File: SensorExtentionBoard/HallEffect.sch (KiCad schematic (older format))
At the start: 11 parts, among them J5 Conn_01x03_Male, J6 Conn_01x03_Male, J7 Conn_01x03_Male, U3 ADS1015IDGS

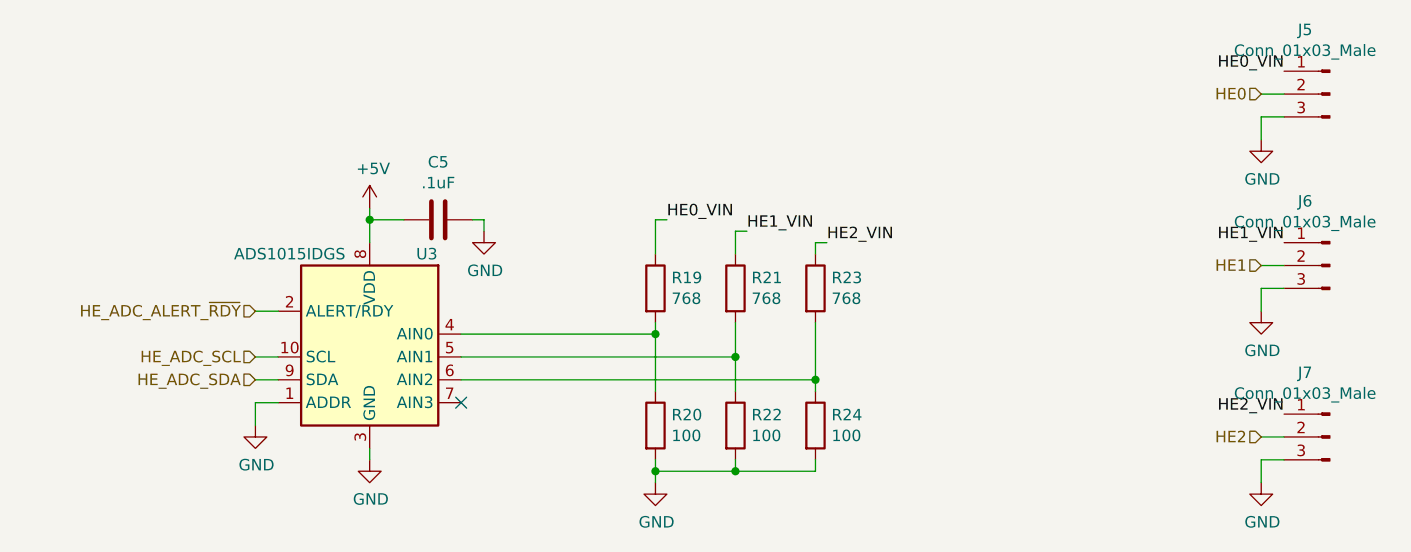
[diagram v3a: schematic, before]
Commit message: Replaced ADS1115 with ADS1015 on PT page
The ADS1115 is being used to read the voltages provided by the Helix
system to the pressure transducers. The ADS1015 is already doing
the same job for the Hall Effect sensors, however the ADS1015 has
4 bits lower accuracy. High accuracy is not needed for this
application so be replacing the ADS1115 with the ADS1015 we can
reduce cost and more importantly reduce BOM size making the project
logistics easier to manage.
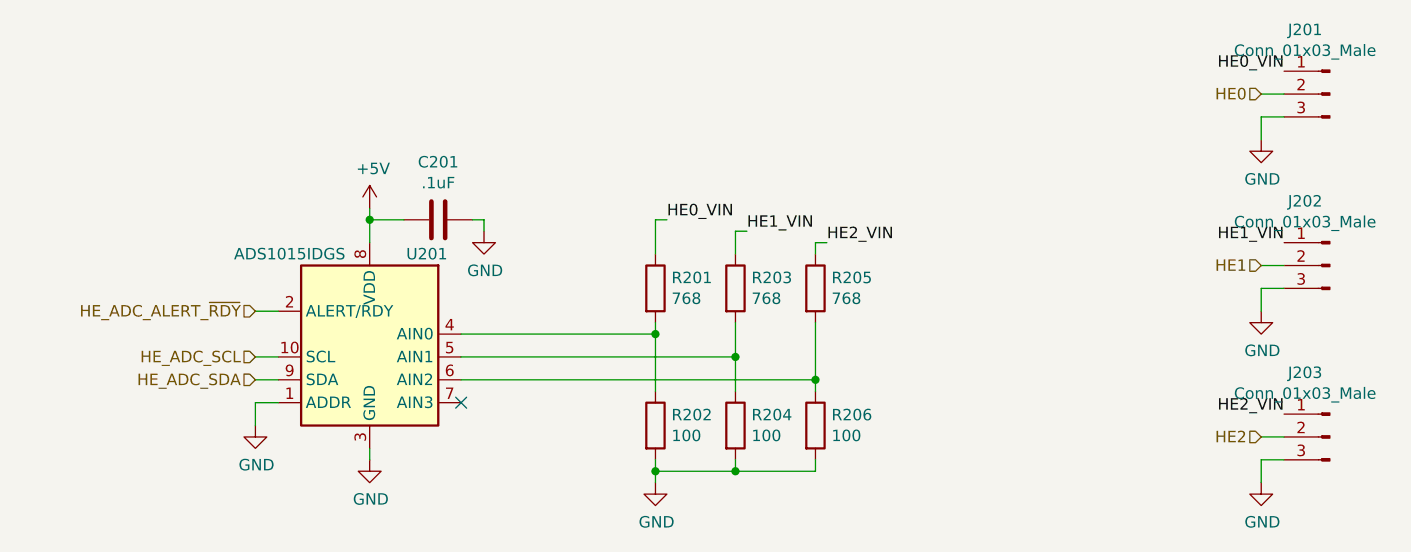
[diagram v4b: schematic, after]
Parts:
- renumbered C5 to C201, J5 to J201, J6 to J202, J7 to J203, R19 to R201, R20 to R202, R21 to R203, R22 to R204, R23 to R205, R24 to R206, U3 to U201
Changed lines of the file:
@@
 $EndDescr
 $Comp
-L Connector:Conn_01x03_Male J5
+L Connector:Conn_01x03_Male J201
 U 1 1 5E39E325
 P 8450 2100
-F 0 "J5" H 8558 2381 50  0000 C CNN
+F 0 "J201" H 8558 2381 50  0000 C CNN
 F 1 "Conn_01x03_Male" H 8558 2290 50  0000 C CNN
 F 2 "Connector_Molex:Molex_MicroClasp_55932-0310_1x03_P2.00mm_Vertical" H 8450 2100 50  0001 C CNN
@@
 $EndComp
 $Comp
-L Analog_ADC:ADS1015IDGS U3
+L Analog_ADC:ADS1015IDGS U201
 U 1 1 5E39F012
 P 4250 3250
-F 0 "U3" H 4000 3700 50  0000 C CNN
+F 0 "U201" H 4000 3700 50  0000 C CNN
 F 1 "ADS1015IDGS" H 4600 3700 50  0000 C CNN
 F 2 "Package_SO:TSSOP-10_3x3mm_P0.5mm" H 4250 2750 50  0001 C CNN
@@
 	8150 2100 8250 2100
 $Comp
-L power:GND #PWR021
+L power:GND #PWR0206
 U 1 1 5E3A1F0E
 P 8150 2300
-F 0 "#PWR021" H 8150 2050 50  0001 C CNN
+F 0 "#PWR0206" H 8150 2050 50  0001 C CNN
 F 1 "GND" H 8155 2127 50  0000 C CNN
 F 2 "" H 8150 2300 50  0001 C CNN
@@
 HE0_VIN
 $Comp
-L Connector:Conn_01x03_Male J6
+L Connector:Conn_01x03_Male J202
 U 1 1 5E3A451B
 P 8450 2850
-F 0 "J6" H 8558 3131 50  0000 C CNN
+F 0 "J202" H 8558 3131 50  0000 C CNN
 F 1 "Conn_01x03_Male" H 8558 3040 50  0000 C CNN
 F 2 "Connector_Molex:Molex_MicroClasp_55932-0310_1x03_P2.00mm_Vertical" H 8450 2850 50  0001 C CNN
@@
 	8150 2850 8250 2850
 $Comp
-L power:GND #PWR022
+L power:GND #PWR0207
 U 1 1 5E3A4523
 P 8150 3050
-F 0 "#PWR022" H 8150 2800 50  0001 C CNN
+F 0 "#PWR0207" H 8150 2800 50  0001 C CNN
 F 1 "GND" H 8155 2877 50  0000 C CNN
 F 2 "" H 8150 3050 50  0001 C CNN
@@
 HE1_VIN
 $Comp
-L Connector:Conn_01x03_Male J7
+L Connector:Conn_01x03_Male J203
 U 1 1 5E3A51E7
 P 8450 3600
-F 0 "J7" H 8558 3881 50  0000 C CNN
+F 0 "J203" H 8558 3881 50  0000 C CNN
 F 1 "Conn_01x03_Male" H 8558 3790 50  0000 C CNN
 F 2 "Connector_Molex:Molex_MicroClasp_55932-0310_1x03_P2.00mm_Vertical" H 8450 3600 50  0001 C CNN
@@
 	8150 3600 8250 3600
 $Comp
-L power:GND #PWR023
+L power:GND #PWR0208
 U 1 1 5E3A51EF
 P 8150 3800
-F 0 "#PWR023" H 8150 3550 50  0001 C CNN
+F 0 "#PWR0208" H 8150 3550 50  0001 C CNN
 F 1 "GND" H 8155 3627 50  0000 C CNN
 F 2 "" H 8150 3800 50  0001 C CNN
@@
 HE2_VIN
 $Comp
-L power:GND #PWR018
+L power:GND #PWR0203
 U 1 1 5E3A708B
 P 4250 3700
-F 0 "#PWR018" H 4250 3450 50  0001 C CNN
+F 0 "#PWR0203" H 4250 3450 50  0001 C CNN
 F 1 "GND" H 4255 3527 50  0000 C CNN
 F 2 "" H 4250 3700 50  0001 C CNN
@@
 	4250 3700 4250 3650
 $Comp
-L power:GND #PWR016
+L power:GND #PWR0201
 U 1 1 5E3A756C
 P 3750 3550
-F 0 "#PWR016" H 3750 3300 50  0001 C CNN
+F 0 "#PWR0201" H 3750 3300 50  0001 C CNN
 F 1 "GND" H 3755 3377 50  0000 C CNN
 F 2 "" H 3750 3550 50  0001 C CNN
@@
 Connection ~ 6200 3350
 $Comp
-L power:GND #PWR020
+L power:GND #PWR0205
 U 1 1 5E3B85EB
 P 5500 3800
-F 0 "#PWR020" H 5500 3550 50  0001 C CNN
+F 0 "#PWR0205" H 5500 3550 50  0001 C CNN
 F 1 "GND" H 5505 3627 50  0000 C CNN
 F 2 "" H 5500 3800 50  0001 C CNN
@@
 	5500 2650 5500 2800
 $Comp
-L power:+5V #PWR017
+L power:+5V #PWR0202
 U 1 1 5E3C2F7A
 P 4250 2600
-F 0 "#PWR017" H 4250 2450 50  0001 C CNN
+F 0 "#PWR0202" H 4250 2450 50  0001 C CNN
 F 1 "+5V" H 4265 2773 50  0000 C CNN
 F 2 "" H 4250 2600 50  0001 C CNN
@@
 P 5500 3550
 AR Path="/5E628041" Ref="R?"  Part="1"
-AR Path="/5E059E7A/5E628041" Ref="R20"  Part="1"
-F 0 "R20" H 5570 3596 50  0000 L CNN
+AR Path="/5E059E7A/5E628041" Ref="R202"  Part="1"
+F 0 "R202" H 5570 3596 50  0000 L CNN
 F 1 "100" H 5570 3505 50  0000 L CNN
 F 2 "Resistor_SMD:R_1206_3216Metric_Pad1.42x1.75mm_HandSolder" V 5430 3550 50  0001 C CNN
@@
 P 6200 2950
 AR Path="/5E059EAC/5E63C1A6" Ref="R?"  Part="1"
-AR Path="/5E059E7A/5E63C1A6" Ref="R23"  Part="1"
-F 0 "R23" H 6270 2996 50  0000 L CNN
+AR Path="/5E059E7A/5E63C1A6" Ref="R205"  Part="1"
+F 0 "R205" H 6270 2996 50  0000 L CNN
 F 1 "768" H 6270 2905 50  0000 L CNN
 F 2 "Resistor_SMD:R_1206_3216Metric_Pad1.42x1.75mm_HandSolder" V 6130 2950 50  0001 C CNN
@@
 P 5850 2950
 AR Path="/5E059EAC/5E63F6B5" Ref="R?"  Part="1"
-AR Path="/5E059E7A/5E63F6B5" Ref="R21"  Part="1"
-F 0 "R21" H 5920 2996 50  0000 L CNN
+AR Path="/5E059E7A/5E63F6B5" Ref="R203"  Part="1"
+F 0 "R203" H 5920 2996 50  0000 L CNN
 F 1 "768" H 5920 2905 50  0000 L CNN
 F 2 "Resistor_SMD:R_1206_3216Metric_Pad1.42x1.75mm_HandSolder" V 5780 2950 50  0001 C CNN
@@
 P 5500 2950
 AR Path="/5E059EAC/5E63FA92" Ref="R?"  Part="1"
-AR Path="/5E059E7A/5E63FA92" Ref="R19"  Part="1"
-F 0 "R19" H 5570 2996 50  0000 L CNN
+AR Path="/5E059E7A/5E63FA92" Ref="R201"  Part="1"
+F 0 "R201" H 5570 2996 50  0000 L CNN
 F 1 "768" H 5570 2905 50  0000 L CNN
 F 2 "Resistor_SMD:R_1206_3216Metric_Pad1.42x1.75mm_HandSolder" V 5430 2950 50  0001 C CNN
@@
 P 5850 3550
 AR Path="/5E6458A4" Ref="R?"  Part="1"
-AR Path="/5E059E7A/5E6458A4" Ref="R22"  Part="1"
-F 0 "R22" H 5920 3596 50  0000 L CNN
+AR Path="/5E059E7A/5E6458A4" Ref="R204"  Part="1"
+F 0 "R204" H 5920 3596 50  0000 L CNN
 F 1 "100" H 5920 3505 50  0000 L CNN
 F 2 "Resistor_SMD:R_1206_3216Metric_Pad1.42x1.75mm_HandSolder" V 5780 3550 50  0001 C CNN
@@
 P 6200 3550
 AR Path="/5E645AA9" Ref="R?"  Part="1"
-AR Path="/5E059E7A/5E645AA9" Ref="R24"  Part="1"
-F 0 "R24" H 6270 3596 50  0000 L CNN
+AR Path="/5E059E7A/5E645AA9" Ref="R206"  Part="1"
+F 0 "R206" H 6270 3596 50  0000 L CNN
 F 1 "100" H 6270 3505 50  0000 L CNN
 F 2 "Resistor_SMD:R_1206_3216Metric_Pad1.42x1.75mm_HandSolder" V 6130 3550 50  0001 C CNN
@@
 P 4550 2650
 AR Path="/5E24F640" Ref="C?"  Part="1"
-AR Path="/5E059E7A/5E24F640" Ref="C5"  Part="1"
-F 0 "C5" V 4298 2650 50  0000 C CNN
+AR Path="/5E059E7A/5E24F640" Ref="C201"  Part="1"
+F 0 "C201" V 4298 2650 50  0000 C CNN
 F 1 ".1uF" V 4389 2650 50  0000 C CNN
 F 2 "" H 4588 2500 50  0001 C CNN
@@
 P 4750 2700
 AR Path="/5E24F646" Ref="#PWR?"  Part="1"
-AR Path="/5E059E7A/5E24F646" Ref="#PWR019"  Part="1"
-F 0 "#PWR019" H 4750 2450 50  0001 C CNN
+AR Path="/5E059E7A/5E24F646" Ref="#PWR0204"  Part="1"
+F 0 "#PWR0204" H 4750 2450 50  0001 C CNN
 F 1 "GND" H 4755 2527 50  0000 C CNN
 F 2 "" H 4750 2700 50  0001 C CNN

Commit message: Added header for programming the EEPROM memory on the SEB
Adding this header may allow the test rig to load new memory configs
onto the SEB under test prior to running tests. This will allow
greater ability for automation of testing when the new software
requires a change to the config onboard the SEB.
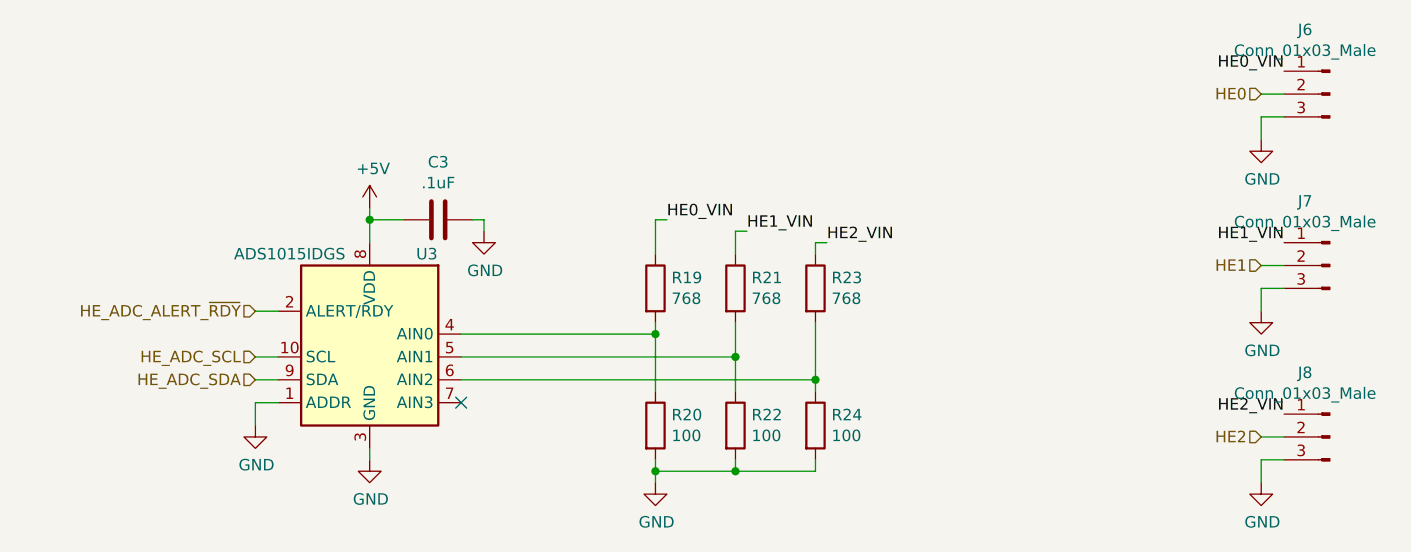
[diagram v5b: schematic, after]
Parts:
- renumbered C201 to C3, J201 to J6, J202 to J7, J203 to J8, R201 to R19, R202 to R20, R203 to R21, R204 to R22, R205 to R23, R206 to R24, U201 to U3
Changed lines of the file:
@@
 $EndDescr
 $Comp
-L Connector:Conn_01x03_Male J201
+L Connector:Conn_01x03_Male J6
 U 1 1 5E39E325
 P 8450 2100
-F 0 "J201" H 8558 2381 50  0000 C CNN
+F 0 "J6" H 8558 2381 50  0000 C CNN
 F 1 "Conn_01x03_Male" H 8558 2290 50  0000 C CNN
 F 2 "Connector_Molex:Molex_MicroClasp_55932-0310_1x03_P2.00mm_Vertical" H 8450 2100 50  0001 C CNN
@@
 $EndComp
 $Comp
-L Analog_ADC:ADS1015IDGS U201
+L Analog_ADC:ADS1015IDGS U3
 U 1 1 5E39F012
 P 4250 3250
-F 0 "U201" H 4000 3700 50  0000 C CNN
+F 0 "U3" H 4000 3700 50  0000 C CNN
 F 1 "ADS1015IDGS" H 4600 3700 50  0000 C CNN
 F 2 "Package_SO:TSSOP-10_3x3mm_P0.5mm" H 4250 2750 50  0001 C CNN
@@
 	8150 2100 8250 2100
 $Comp
-L power:GND #PWR0206
+L power:GND #PWR024
 U 1 1 5E3A1F0E
 P 8150 2300
-F 0 "#PWR0206" H 8150 2050 50  0001 C CNN
+F 0 "#PWR024" H 8150 2050 50  0001 C CNN
 F 1 "GND" H 8155 2127 50  0000 C CNN
 F 2 "" H 8150 2300 50  0001 C CNN
@@
 HE0_VIN
 $Comp
-L Connector:Conn_01x03_Male J202
+L Connector:Conn_01x03_Male J7
 U 1 1 5E3A451B
 P 8450 2850
-F 0 "J202" H 8558 3131 50  0000 C CNN
+F 0 "J7" H 8558 3131 50  0000 C CNN
 F 1 "Conn_01x03_Male" H 8558 3040 50  0000 C CNN
 F 2 "Connector_Molex:Molex_MicroClasp_55932-0310_1x03_P2.00mm_Vertical" H 8450 2850 50  0001 C CNN
@@
 	8150 2850 8250 2850
 $Comp
-L power:GND #PWR0207
+L power:GND #PWR025
 U 1 1 5E3A4523
 P 8150 3050
-F 0 "#PWR0207" H 8150 2800 50  0001 C CNN
+F 0 "#PWR025" H 8150 2800 50  0001 C CNN
 F 1 "GND" H 8155 2877 50  0000 C CNN
 F 2 "" H 8150 3050 50  0001 C CNN
@@
 HE1_VIN
 $Comp
-L Connector:Conn_01x03_Male J203
+L Connector:Conn_01x03_Male J8
 U 1 1 5E3A51E7
 P 8450 3600
-F 0 "J203" H 8558 3881 50  0000 C CNN
+F 0 "J8" H 8558 3881 50  0000 C CNN
 F 1 "Conn_01x03_Male" H 8558 3790 50  0000 C CNN
 F 2 "Connector_Molex:Molex_MicroClasp_55932-0310_1x03_P2.00mm_Vertical" H 8450 3600 50  0001 C CNN
@@
 	8150 3600 8250 3600
 $Comp
-L power:GND #PWR0208
+L power:GND #PWR026
 U 1 1 5E3A51EF
 P 8150 3800
-F 0 "#PWR0208" H 8150 3550 50  0001 C CNN
+F 0 "#PWR026" H 8150 3550 50  0001 C CNN
 F 1 "GND" H 8155 3627 50  0000 C CNN
 F 2 "" H 8150 3800 50  0001 C CNN
@@
 HE2_VIN
 $Comp
-L power:GND #PWR0203
+L power:GND #PWR021
 U 1 1 5E3A708B
 P 4250 3700
-F 0 "#PWR0203" H 4250 3450 50  0001 C CNN
+F 0 "#PWR021" H 4250 3450 50  0001 C CNN
 F 1 "GND" H 4255 3527 50  0000 C CNN
 F 2 "" H 4250 3700 50  0001 C CNN
@@
 	4250 3700 4250 3650
 $Comp
-L power:GND #PWR0201
+L power:GND #PWR019
 U 1 1 5E3A756C
 P 3750 3550
-F 0 "#PWR0201" H 3750 3300 50  0001 C CNN
+F 0 "#PWR019" H 3750 3300 50  0001 C CNN
 F 1 "GND" H 3755 3377 50  0000 C CNN
 F 2 "" H 3750 3550 50  0001 C CNN
@@
 Connection ~ 6200 3350
 $Comp
-L power:GND #PWR0205
+L power:GND #PWR023
 U 1 1 5E3B85EB
 P 5500 3800
-F 0 "#PWR0205" H 5500 3550 50  0001 C CNN
+F 0 "#PWR023" H 5500 3550 50  0001 C CNN
 F 1 "GND" H 5505 3627 50  0000 C CNN
 F 2 "" H 5500 3800 50  0001 C CNN
@@
 	5500 2650 5500 2800
 $Comp
-L power:+5V #PWR0202
+L power:+5V #PWR020
 U 1 1 5E3C2F7A
 P 4250 2600
-F 0 "#PWR0202" H 4250 2450 50  0001 C CNN
+F 0 "#PWR020" H 4250 2450 50  0001 C CNN
 F 1 "+5V" H 4265 2773 50  0000 C CNN
 F 2 "" H 4250 2600 50  0001 C CNN
@@
 P 5500 3550
 AR Path="/5E628041" Ref="R?"  Part="1"
-AR Path="/5E059E7A/5E628041" Ref="R202"  Part="1"
-F 0 "R202" H 5570 3596 50  0000 L CNN
+AR Path="/5E059E7A/5E628041" Ref="R20"  Part="1"
+F 0 "R20" H 5570 3596 50  0000 L CNN
 F 1 "100" H 5570 3505 50  0000 L CNN
 F 2 "Resistor_SMD:R_1206_3216Metric_Pad1.42x1.75mm_HandSolder" V 5430 3550 50  0001 C CNN
@@
 P 6200 2950
 AR Path="/5E059EAC/5E63C1A6" Ref="R?"  Part="1"
-AR Path="/5E059E7A/5E63C1A6" Ref="R205"  Part="1"
-F 0 "R205" H 6270 2996 50  0000 L CNN
+AR Path="/5E059E7A/5E63C1A6" Ref="R23"  Part="1"
+F 0 "R23" H 6270 2996 50  0000 L CNN
 F 1 "768" H 6270 2905 50  0000 L CNN
 F 2 "Resistor_SMD:R_1206_3216Metric_Pad1.42x1.75mm_HandSolder" V 6130 2950 50  0001 C CNN
@@
 P 5850 2950
 AR Path="/5E059EAC/5E63F6B5" Ref="R?"  Part="1"
-AR Path="/5E059E7A/5E63F6B5" Ref="R203"  Part="1"
-F 0 "R203" H 5920 2996 50  0000 L CNN
+AR Path="/5E059E7A/5E63F6B5" Ref="R21"  Part="1"
+F 0 "R21" H 5920 2996 50  0000 L CNN
 F 1 "768" H 5920 2905 50  0000 L CNN
 F 2 "Resistor_SMD:R_1206_3216Metric_Pad1.42x1.75mm_HandSolder" V 5780 2950 50  0001 C CNN
@@
 P 5500 2950
 AR Path="/5E059EAC/5E63FA92" Ref="R?"  Part="1"
-AR Path="/5E059E7A/5E63FA92" Ref="R201"  Part="1"
-F 0 "R201" H 5570 2996 50  0000 L CNN
+AR Path="/5E059E7A/5E63FA92" Ref="R19"  Part="1"
+F 0 "R19" H 5570 2996 50  0000 L CNN
 F 1 "768" H 5570 2905 50  0000 L CNN
 F 2 "Resistor_SMD:R_1206_3216Metric_Pad1.42x1.75mm_HandSolder" V 5430 2950 50  0001 C CNN
@@
 P 5850 3550
 AR Path="/5E6458A4" Ref="R?"  Part="1"
-AR Path="/5E059E7A/5E6458A4" Ref="R204"  Part="1"
-F 0 "R204" H 5920 3596 50  0000 L CNN
+AR Path="/5E059E7A/5E6458A4" Ref="R22"  Part="1"
+F 0 "R22" H 5920 3596 50  0000 L CNN
 F 1 "100" H 5920 3505 50  0000 L CNN
 F 2 "Resistor_SMD:R_1206_3216Metric_Pad1.42x1.75mm_HandSolder" V 5780 3550 50  0001 C CNN
@@
 P 6200 3550
 AR Path="/5E645AA9" Ref="R?"  Part="1"
-AR Path="/5E059E7A/5E645AA9" Ref="R206"  Part="1"
-F 0 "R206" H 6270 3596 50  0000 L CNN
+AR Path="/5E059E7A/5E645AA9" Ref="R24"  Part="1"
+F 0 "R24" H 6270 3596 50  0000 L CNN
 F 1 "100" H 6270 3505 50  0000 L CNN
 F 2 "Resistor_SMD:R_1206_3216Metric_Pad1.42x1.75mm_HandSolder" V 6130 3550 50  0001 C CNN
@@
 P 4550 2650
 AR Path="/5E24F640" Ref="C?"  Part="1"
-AR Path="/5E059E7A/5E24F640" Ref="C201"  Part="1"
-F 0 "C201" V 4298 2650 50  0000 C CNN
+AR Path="/5E059E7A/5E24F640" Ref="C3"  Part="1"
+F 0 "C3" V 4298 2650 50  0000 C CNN
 F 1 ".1uF" V 4389 2650 50  0000 C CNN
 F 2 "" H 4588 2500 50  0001 C CNN
@@
 P 4750 2700
 AR Path="/5E24F646" Ref="#PWR?"  Part="1"
-AR Path="/5E059E7A/5E24F646" Ref="#PWR0204"  Part="1"
-F 0 "#PWR0204" H 4750 2450 50  0001 C CNN
+AR Path="/5E059E7A/5E24F646" Ref="#PWR022"  Part="1"
+F 0 "#PWR022" H 4750 2450 50  0001 C CNN
 F 1 "GND" H 4755 2527 50  0000 C CNN
 F 2 "" H 4750 2700 50  0001 C CNN

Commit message: Changed component footprints to conform to RP standard components
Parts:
- C3: footprint (none) -> Capacitor_SMD:C_1206_3216Metric_Pad1.42x1.75mm_HandSolder
- J6, J7, J8: footprint Connector_Molex:Molex_MicroClasp_55932-0310_1x03_P2.00mm_Vertical -> Connector_Molex:Molex_MicroClasp_55932-0330_1x03_P2.00mm_Vertical
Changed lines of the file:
@@
 encoding utf-8
 Sheet 2 5
-Title ""
-Date ""
-Rev ""
-Comp ""
-Comment1 ""
+Title "Helix Test Rig SEB"
+Date "2020-01-14"
+Rev "1.0.0"
+Comp "SDSU Rocket Project"
+Comment1 "Schematic Design: David Knight"
 Comment2 ""
 Comment3 ""
@@
 F 0 "J6" H 8558 2381 50  0000 C CNN
 F 1 "Conn_01x03_Male" H 8558 2290 50  0000 C CNN
-F 2 "Connector_Molex:Molex_MicroClasp_55932-0310_1x03_P2.00mm_Vertical" H 8450 2100 50  0001 C CNN
+F 2 "Connector_Molex:Molex_MicroClasp_55932-0330_1x03_P2.00mm_Vertical" H 8450 2100 50  0001 C CNN
 F 3 "~" H 8450 2100 50  0001 C CNN
 	1    8450 2100
@@
 	8150 2100 8250 2100
 $Comp
-L power:GND #PWR024
+L power:GND #PWR027
 U 1 1 5E3A1F0E
 P 8150 2300
-F 0 "#PWR024" H 8150 2050 50  0001 C CNN
+F 0 "#PWR027" H 8150 2050 50  0001 C CNN
 F 1 "GND" H 8155 2127 50  0000 C CNN
 F 2 "" H 8150 2300 50  0001 C CNN
@@
 F 0 "J7" H 8558 3131 50  0000 C CNN
 F 1 "Conn_01x03_Male" H 8558 3040 50  0000 C CNN
-F 2 "Connector_Molex:Molex_MicroClasp_55932-0310_1x03_P2.00mm_Vertical" H 8450 2850 50  0001 C CNN
+F 2 "Connector_Molex:Molex_MicroClasp_55932-0330_1x03_P2.00mm_Vertical" H 8450 2850 50  0001 C CNN
 F 3 "~" H 8450 2850 50  0001 C CNN
 	1    8450 2850
@@
 	8150 2850 8250 2850
 $Comp
-L power:GND #PWR025
+L power:GND #PWR028
 U 1 1 5E3A4523
 P 8150 3050
-F 0 "#PWR025" H 8150 2800 50  0001 C CNN
+F 0 "#PWR028" H 8150 2800 50  0001 C CNN
 F 1 "GND" H 8155 2877 50  0000 C CNN
 F 2 "" H 8150 3050 50  0001 C CNN
@@
 F 0 "J8" H 8558 3881 50  0000 C CNN
 F 1 "Conn_01x03_Male" H 8558 3790 50  0000 C CNN
-F 2 "Connector_Molex:Molex_MicroClasp_55932-0310_1x03_P2.00mm_Vertical" H 8450 3600 50  0001 C CNN
+F 2 "Connector_Molex:Molex_MicroClasp_55932-0330_1x03_P2.00mm_Vertical" H 8450 3600 50  0001 C CNN
 F 3 "~" H 8450 3600 50  0001 C CNN
 	1    8450 3600
@@
 	8150 3600 8250 3600
 $Comp
-L power:GND #PWR026
+L power:GND #PWR029
 U 1 1 5E3A51EF
 P 8150 3800
-F 0 "#PWR026" H 8150 3550 50  0001 C CNN
+F 0 "#PWR029" H 8150 3550 50  0001 C CNN
 F 1 "GND" H 8155 3627 50  0000 C CNN
 F 2 "" H 8150 3800 50  0001 C CNN
@@
 HE2_VIN
 $Comp
-L power:GND #PWR021
+L power:GND #PWR024
 U 1 1 5E3A708B
 P 4250 3700
-F 0 "#PWR021" H 4250 3450 50  0001 C CNN
+F 0 "#PWR024" H 4250 3450 50  0001 C CNN
 F 1 "GND" H 4255 3527 50  0000 C CNN
 F 2 "" H 4250 3700 50  0001 C CNN
@@
 	4250 3700 4250 3650
 $Comp
-L power:GND #PWR019
+L power:GND #PWR022
 U 1 1 5E3A756C
 P 3750 3550
-F 0 "#PWR019" H 3750 3300 50  0001 C CNN
+F 0 "#PWR022" H 3750 3300 50  0001 C CNN
 F 1 "GND" H 3755 3377 50  0000 C CNN
 F 2 "" H 3750 3550 50  0001 C CNN
@@
 Connection ~ 6200 3350
 $Comp
-L power:GND #PWR023
+L power:GND #PWR026
 U 1 1 5E3B85EB
 P 5500 3800
-F 0 "#PWR023" H 5500 3550 50  0001 C CNN
+F 0 "#PWR026" H 5500 3550 50  0001 C CNN
 F 1 "GND" H 5505 3627 50  0000 C CNN
 F 2 "" H 5500 3800 50  0001 C CNN
@@
 	5500 2650 5500 2800
 $Comp
-L power:+5V #PWR020
+L power:+5V #PWR023
 U 1 1 5E3C2F7A
 P 4250 2600
-F 0 "#PWR020" H 4250 2450 50  0001 C CNN
+F 0 "#PWR023" H 4250 2450 50  0001 C CNN
 F 1 "+5V" H 4265 2773 50  0000 C CNN
 F 2 "" H 4250 2600 50  0001 C CNN
@@
 F 0 "C3" V 4298 2650 50  0000 C CNN
 F 1 ".1uF" V 4389 2650 50  0000 C CNN
-F 2 "" H 4588 2500 50  0001 C CNN
+F 2 "Capacitor_SMD:C_1206_3216Metric_Pad1.42x1.75mm_HandSolder" H 4588 2500 50  0001 C CNN
 F 3 "~" H 4550 2650 50  0001 C CNN
 	1    4550 2650
@@
 P 4750 2700
 AR Path="/5E24F646" Ref="#PWR?"  Part="1"
-AR Path="/5E059E7A/5E24F646" Ref="#PWR022"  Part="1"
-F 0 "#PWR022" H 4750 2450 50  0001 C CNN
+AR Path="/5E059E7A/5E24F646" Ref="#PWR025"  Part="1"
+F 0 "#PWR025" H 4750 2450 50  0001 C CNN
 F 1 "GND" H 4755 2527 50  0000 C CNN
 F 2 "" H 4750 2700 50  0001 C CNN
